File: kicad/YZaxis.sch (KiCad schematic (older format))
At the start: 36 parts, among them CON16 YZ, CON17 Stepstick_Left_Connector, CON18 Stepstick_Right_Connector, CON19 Stepstick_Left_Connector, CON20 Stepstick_Right_Connector, Q5 IRLR2905ZPBF, Q6 FDC6401N, U1 CD4504BPW

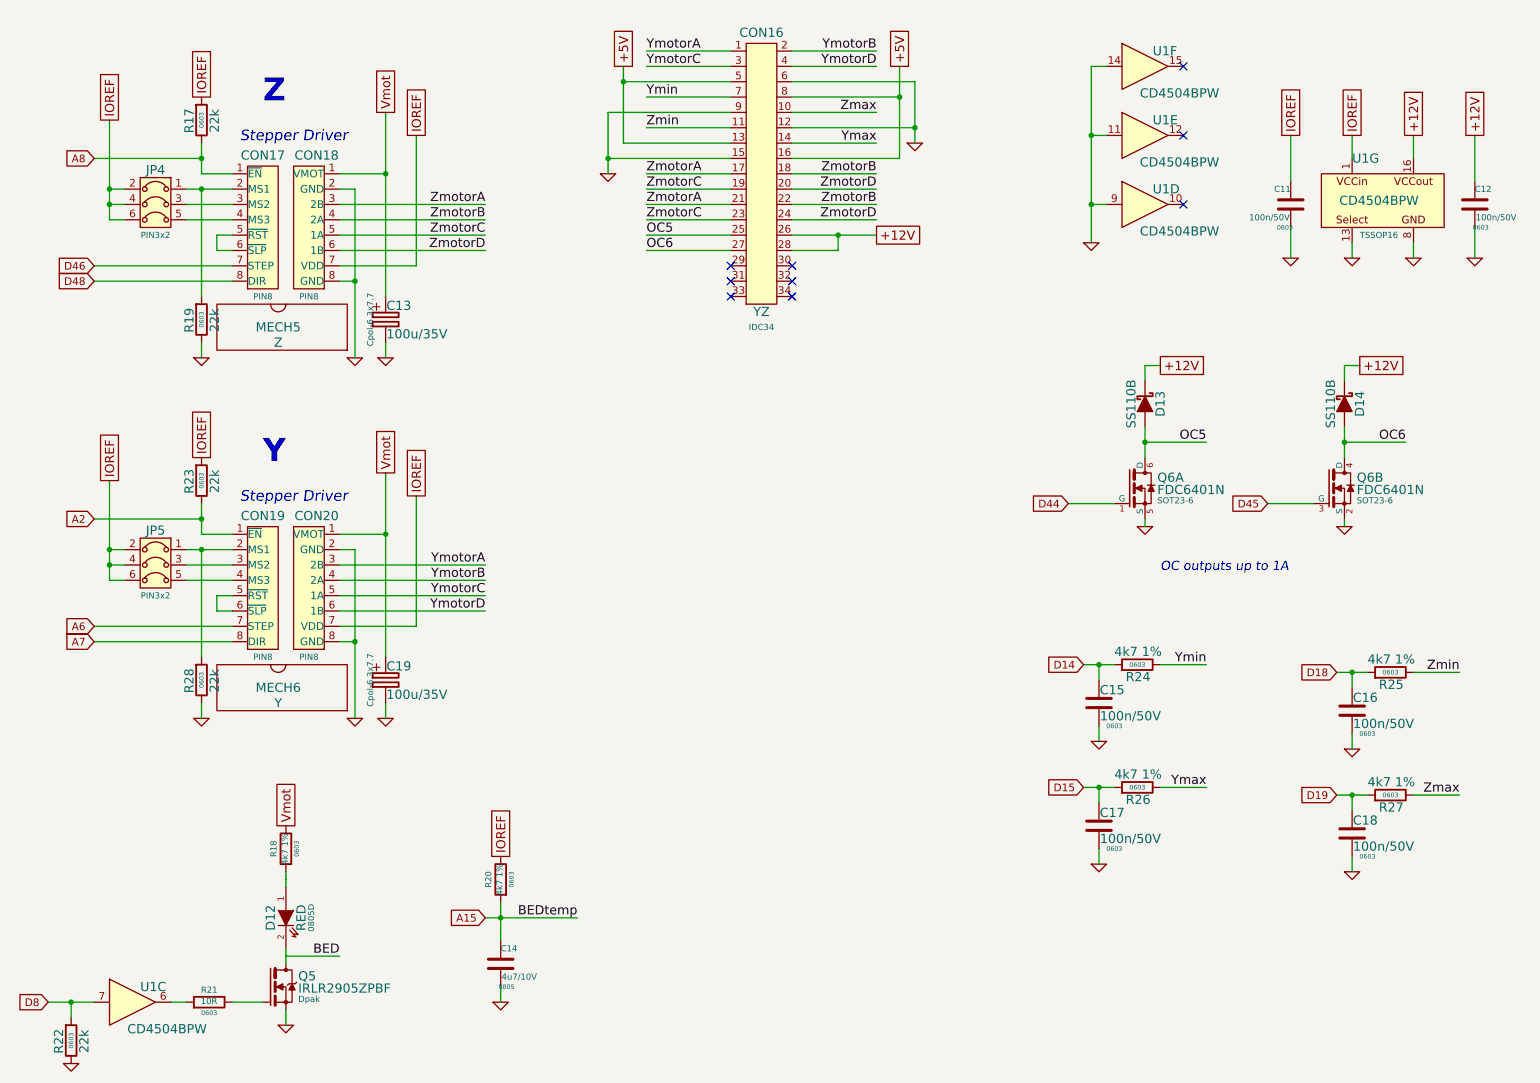
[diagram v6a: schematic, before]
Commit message: Add bed connector. Routing.
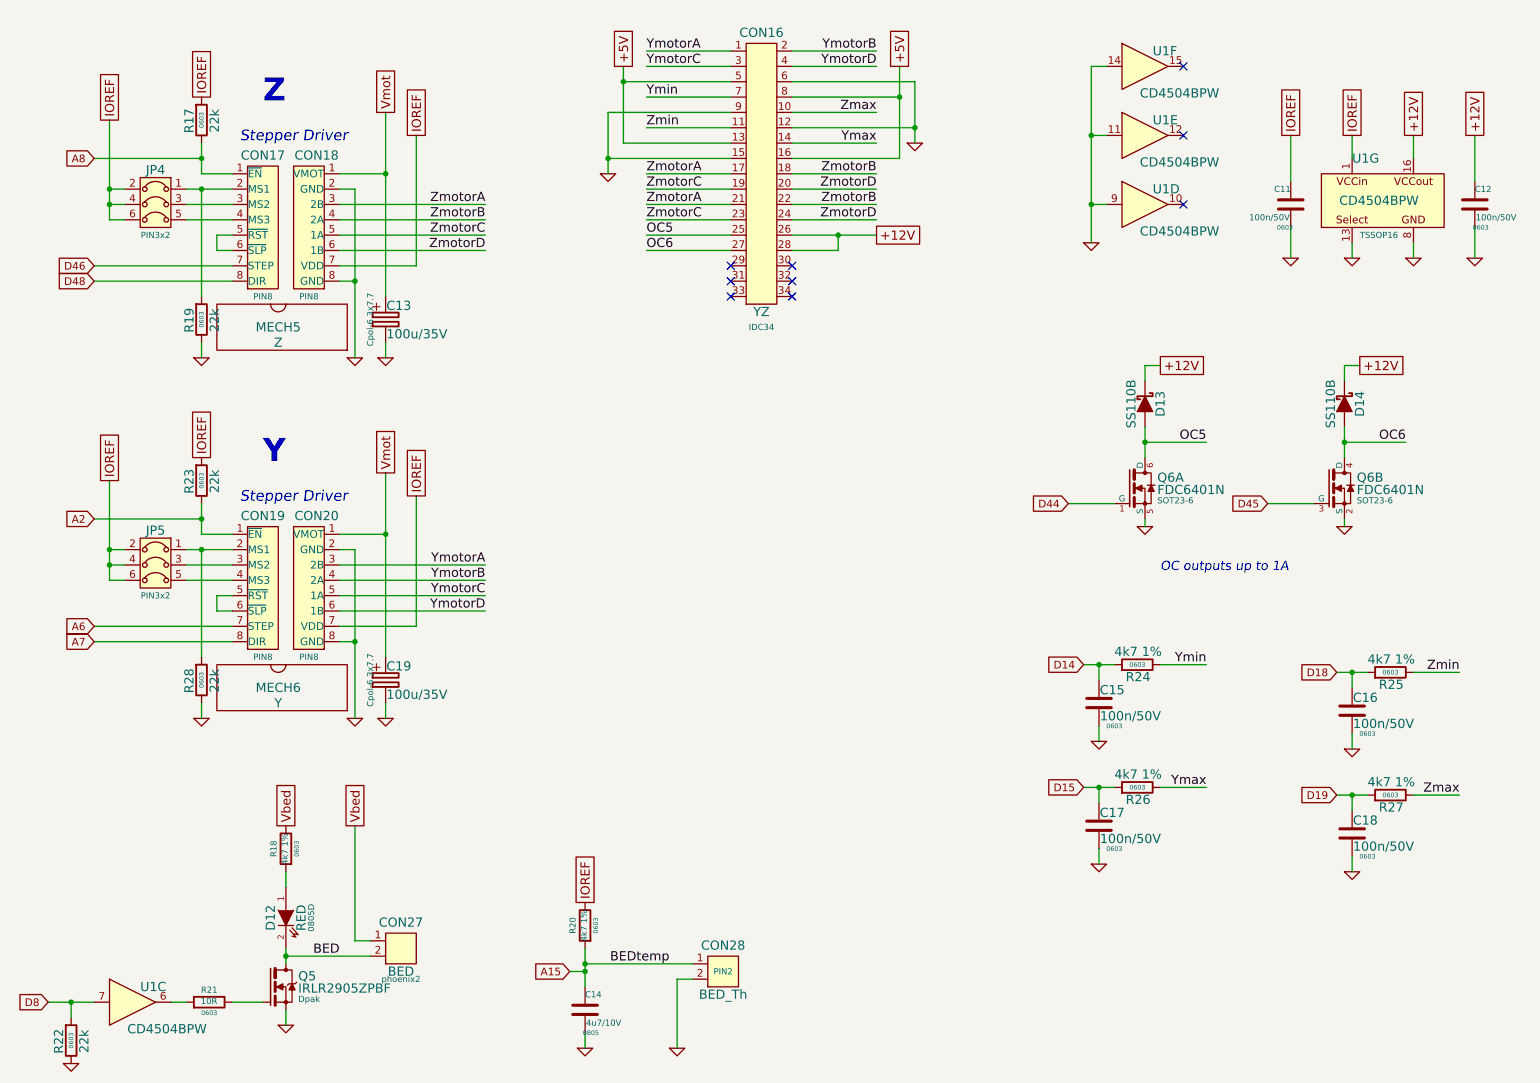
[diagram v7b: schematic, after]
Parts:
- added CON27: BED, phoenix2, symbol CON2
- added CON28: BED_Th, PIN2, symbol CON2
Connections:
- net A15: now also CON28.1
- net BED: now also D12.2 (K), Q5.4 (D), CON27.2
- net GND: now also CON28.2
- net Vmot: no longer R18.2
- new net Vbed: CON27.1, R18.2
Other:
- moved on the sheet: C14, R20
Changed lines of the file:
@@
 L R R20
 U 1 1 534ECA59
-P 3950 6300
-F 0 "R20" V 4030 6300 40  0000 C CNN
-F 1 "4k7 1%" V 3957 6301 40  0000 C CNN
-F 2 "0603" V 3880 6300 30  0000 C CNN
-F 3 "~" H 3950 6300 30  0000 C CNN
-	1    3950 6300
+P 4500 6600
+F 0 "R20" V 4580 6600 40  0000 C CNN
+F 1 "4k7 1%" V 4507 6601 40  0000 C CNN
+F 2 "0603" V 4430 6600 30  0000 C CNN
+F 3 "~" H 4500 6600 30  0000 C CNN
+	1    4500 6600
 	-1   0    0    1
 $EndComp
@@
 L C C14
 U 1 1 534ECB63
-P 3950 6850
-F 0 "C14" H 3950 6950 40  0000 L CNN
-F 1 "4u7/10V" H 3956 6765 40  0000 L CNN
-F 2 "0805" H 3988 6700 30  0000 C CNN
-F 3 "~" H 3950 6850 60  0000 C CNN
-	1    3950 6850
+P 4500 7150
+F 0 "C14" H 4500 7250 40  0000 L CNN
+F 1 "4u7/10V" H 4506 7065 40  0000 L CNN
+F 2 "0805" H 4538 7000 30  0000 C CNN
+F 3 "~" H 4500 7150 60  0000 C CNN
+	1    4500 7150
 	1    0    0    -1
 $EndComp
@@
 L GND #PWR028
 U 1 1 534ECB96
-P 3950 7100
-F 0 "#PWR028" H 3950 7100 30  0001 C CNN
-F 1 "GND" H 3950 7030 30  0001 C CNN
-F 2 "~" H 3950 7100 60  0000 C CNN
-F 3 "~" H 3950 7100 60  0000 C CNN
-	1    3950 7100
-	1    0    0    -1
-$EndComp
-Wire Wire Line
-	3950 7100 3950 7000
-Wire Wire Line
-	3950 6450 3950 6550
-Wire Wire Line
-	3950 6550 3950 6700
-Text GLabel 3850 6550 0    50   Input ~ 0
+P 4500 7400
+F 0 "#PWR028" H 4500 7400 30  0001 C CNN
+F 1 "GND" H 4500 7330 30  0001 C CNN
+F 2 "~" H 4500 7400 60  0000 C CNN
+F 3 "~" H 4500 7400 60  0000 C CNN
+	1    4500 7400
+	1    0    0    -1
+$EndComp
+Wire Wire Line
+	4500 7400 4500 7300
+Wire Wire Line
+	4500 6750 4500 7000
+Text GLabel 4400 6900 0    50   Input ~ 0
 A15
-Wire Wire Line
-	3850 6550 3950 6550
-Wire Wire Line
-	3950 6550 4450 6550
-Connection ~ 3950 6550
+Connection ~ 4500 6850
 $Comp
 L GND #PWR029
@@
 $EndComp
 Wire Wire Line
-	2550 6350 2550 6300
-Wire Wire Line
-	2550 6300 2550 6250
+	2550 6250 2550 6350
 Wire Wire Line
 	2550 6850 2550 6750
@@
 +12V
 Text GLabel 2550 5950 1    60   UnSpc ~ 0
-Vmot
+Vbed
 Text GLabel 9500 1450 1    60   UnSpc ~ 0
 IOREF
 Text GLabel 9100 1450 1    60   UnSpc ~ 0
 IOREF
-Text GLabel 3950 6150 1    60   UnSpc ~ 0
+Text GLabel 4500 6450 1    60   UnSpc ~ 0
 IOREF
 Text Label 3850 4250 2    60   ~ 0
@@
 $EndComp
 Wire Wire Line
-	1000 7100 1150 7100
-Wire Wire Line
-	1150 7100 1300 7100
+	1000 7100 1300 7100
 $Comp
 L GND #PWR032
@@
 $EndComp
 Wire Wire Line
-	7750 4900 7850 4900
-Wire Wire Line
-	7850 4900 7950 4900
+	7750 4900 7950 4900
 Wire Wire Line
 	8250 4900 8550 4900
@@
 $EndComp
 Wire Wire Line
-	7750 5700 7850 5700
-Wire Wire Line
-	7850 5700 7950 5700
+	7750 5700 7950 5700
 Wire Wire Line
 	8250 5700 8550 5700
@@
 $EndComp
 Wire Wire Line
-	9400 4950 9500 4950
-Wire Wire Line
-	9500 4950 9600 4950
+	9400 4950 9600 4950
 Wire Wire Line
 	9900 4950 10200 4950
@@
 $EndComp
 Wire Wire Line
-	9400 5750 9500 5750
-Wire Wire Line
-	9500 5750 9600 5750
+	9400 5750 9600 5750
 Wire Wire Line
 	9900 5750 10200 5750
@@
 	5850 1300 6400 1300
 Wire Wire Line
-	5850 1600 6550 1600
+	6550 1600 5850 1600
 Wire Wire Line
 	6400 1500 5850 1500
@@
 Ymin
 Wire Wire Line
-	4750 1000 4750 1100
-Wire Wire Line
-	4750 1100 4750 1500
+	4750 1000 4750 1500
 $Comp
 L GND #PWR038
@@
 $EndComp
 Wire Wire Line
-	4650 1300 4650 1600
-Wire Wire Line
-	4650 1600 4650 1700
+	4650 1300 4650 1700
 Text Label 6400 1300 2    60   ~ 0
 Zmax
 Wire Wire Line
-	6650 1100 6650 1400
-Wire Wire Line
-	6650 1400 6650 1500
+	6650 1100 6650 1500
 Text Label 4900 1400 0    60   ~ 0
 Zmin
@@
 Ymax
 Wire Wire Line
-	6550 1600 6550 1200
-Wire Wire Line
-	6550 1200 6550 1000
+	6550 1000 6550 1600
 Text Label 4900 1900 0    60   ~ 0
 ZmotorA
@@
 +12V
 Wire Wire Line
-	6400 2100 6150 2100
-Wire Wire Line
-	6150 2100 5850 2100
+	5850 2100 6400 2100
 Wire Wire Line
 	5850 2200 6150 2200
@@
 	7900 1000 7800 1000
 Wire Wire Line
-	7800 1000 7800 1450
-Wire Wire Line
-	7800 1450 7800 1900
-Wire Wire Line
-	7800 1900 7800 2150
+	7800 1000 7800 2150
 Wire Wire Line
 	7900 1900 7800 1900
@@
 	9450 4000 9450 3950
 Wire Wire Line
-	8150 3350 8150 3450
-Wire Wire Line
-	8150 3450 8150 3550
-Wire Wire Line
-	9450 3350 9450 3450
-Wire Wire Line
-	9450 3450 9450 3550
+	8150 3350 8150 3550
+Wire Wire Line
+	9450 3350 9450 3550
 Text GLabel 8250 2950 2    60   UnSpc ~ 0
 +12V
@@
 	2000 1700 2200 1700
 Wire Wire Line
-	1900 1800 2000 1800
-Wire Wire Line
-	2000 1800 2200 1800
+	1900 1800 2200 1800
 Wire Wire Line
 	2200 1900 1900 1900
@@
 	2900 2400 3000 2400
 Wire Wire Line
-	3000 1800 3000 2400
-Wire Wire Line
-	3000 2400 3000 2900
+	3000 1800 3000 2900
 Wire Wire Line
 	3000 1800 2900 1800
@@
 	2900 1700 3200 1700
 Wire Wire Line
-	3200 1300 3200 1700
-Wire Wire Line
-	3200 1700 3200 2500
+	3200 1300 3200 2500
 Wire Wire Line
 	2900 2300 3400 2300
@@
 	3400 2300 3400 1450
 Wire Wire Line
-	2000 1500 2000 1600
-Wire Wire Line
-	2000 1600 2000 1700
+	2000 1500 2000 1700
 Wire Wire Line
 	1300 1600 2000 1600
@@
 	1400 2000 1500 2000
 Wire Wire Line
-	1400 1350 1400 1800
-Wire Wire Line
-	1400 1800 1400 1900
-Wire Wire Line
-	1400 1900 1400 2000
+	1400 1350 1400 2000
 Wire Wire Line
 	1500 1800 1400 1800
@@
 	2000 4050 2200 4050
 Wire Wire Line
-	1900 4150 2000 4150
-Wire Wire Line
-	2000 4150 2200 4150
+	1900 4150 2200 4150
 Wire Wire Line
 	2200 4250 1900 4250
@@
 	2900 4750 3000 4750
 Wire Wire Line
-	3000 4150 3000 4750
-Wire Wire Line
-	3000 4750 3000 5250
+	3000 4150 3000 5250
 Wire Wire Line
 	3000 4150 2900 4150
@@
 	2900 4050 3200 4050
 Wire Wire Line
-	3200 3650 3200 4050
-Wire Wire Line
-	3200 4050 3200 4850
+	3200 3650 3200 4850
 Wire Wire Line
 	2900 4650 3400 4650
@@
 	3400 4650 3400 3800
 Wire Wire Line
-	2000 3850 2000 3950
-Wire Wire Line
-	2000 3950 2000 4050
+	2000 3850 2000 4050
 Wire Wire Line
 	1300 3950 2000 3950
@@
 	1400 4350 1500 4350
 Wire Wire Line
-	1400 3700 1400 4150
-Wire Wire Line
-	1400 4150 1400 4250
-Wire Wire Line
-	1400 4250 1400 4350
+	1400 3700 1400 4350
 Wire Wire Line
 	1500 4150 1400 4150
@@
 	1    0    0    -1
 $EndComp
-Wire Wire Line
-	2550 6800 2900 6800
 Text Label 2900 6800 2    60   ~ 0
 BED
-Text Label 4450 6550 2    60   ~ 0
+Text Label 5050 6850 2    60   ~ 0
 BEDtemp
+$Comp
+L CON2 CON28
+U 1 1 539C896C
+P 5400 6900
+F 0 "CON28" H 5400 7070 60  0000 C CNN
+F 1 "BED_Th" H 5400 6750 60  0000 C CNN
+F 2 "PIN2" H 5400 6900 40  0000 C CNN
+F 3 "" H 5400 6900 40  0000 C CNN
+	1    5400 6900
+	1    0    0    -1
+$EndComp
+$Comp
+L CON2 CON27
+U 1 1 539C8A5D
+P 3300 6750
+F 0 "CON27" H 3300 6920 60  0000 C CNN
+F 1 "BED" H 3300 6600 60  0000 C CNN
+F 2 "phoenix2" H 3300 6550 40  0000 C CNN
+F 3 "" H 3300 6750 40  0000 C CNN
+	1    3300 6750
+	1    0    0    -1
+$EndComp
+Wire Wire Line
+	5200 6950 5100 6950
+Wire Wire Line
+	5100 6950 5100 7400
+$Comp
+L GND #PWR049
+U 1 1 539C8F1D
+P 5100 7400
+F 0 "#PWR049" H 5100 7400 30  0001 C CNN
+F 1 "GND" H 5100 7330 30  0001 C CNN
+F 2 "~" H 5100 7400 60  0000 C CNN
+F 3 "~" H 5100 7400 60  0000 C CNN
+	1    5100 7400
+	1    0    0    -1
+$EndComp
+Wire Wire Line
+	3100 6700 3000 6700
+Wire Wire Line
+	3000 6700 3000 5950
+Text GLabel 3000 5950 1    60   UnSpc ~ 0
+Vbed
+Wire Wire Line
+	3100 6800 2550 6800
+Connection ~ 2550 6800
+Wire Wire Line
+	4500 6850 5200 6850
+Wire Wire Line
+	4400 6900 4500 6900
+Connection ~ 4500 6900
 $EndSCHEMATC

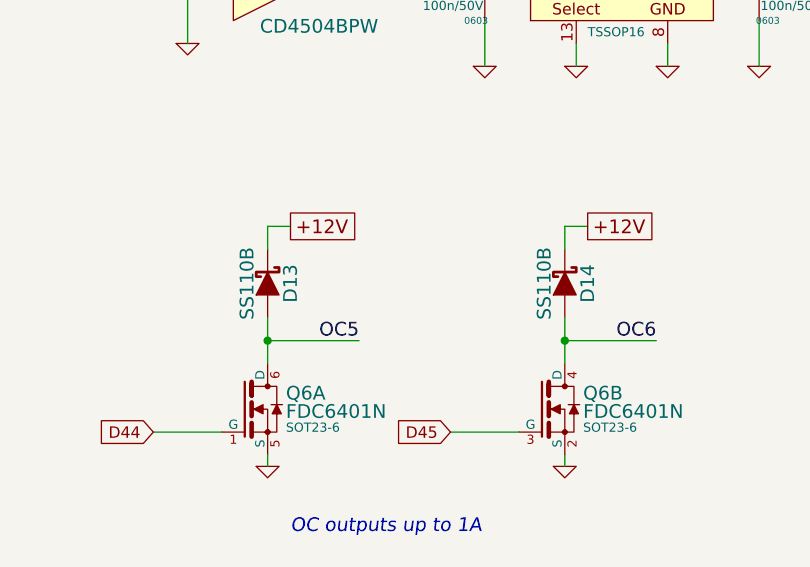
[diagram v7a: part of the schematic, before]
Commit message: Change 1A diodes. Add capacitors next to OC outputs. Place.
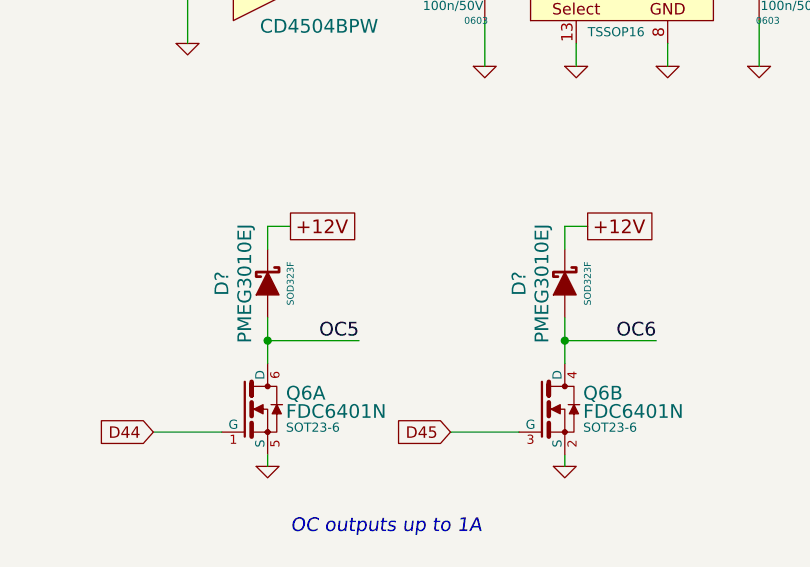
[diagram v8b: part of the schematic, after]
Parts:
- removed D13, D14: SS110B, symbol SS110B
- added D? (x2): PMEG3010EJ, SOD323F, symbol PMEG3010EJ
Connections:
- net +12V: now also D?.1, D?.1
- net OC5: now also D?.2
- net OC6: now also D?.2
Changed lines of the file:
@@
 Text GLabel 8250 2950 2    60   UnSpc ~ 0
 +12V
-$Comp
-L SS110B D13
-U 1 1 53924625
-P 8150 3200
-F 0 "D13" H 8150 3100 60  0000 C CNN
-F 1 "SS110B" H 8150 3290 60  0000 C CNN
-F 2 "" V 8000 3162 30  0000 C CNN
-F 3 "" V 8150 3200 60  0000 C CNN
-	1    8150 3200
-	0    -1   -1   0
-$EndComp
 Wire Wire Line
 	8250 2950 8150 2950
@@
 Text GLabel 9550 2950 2    60   UnSpc ~ 0
 +12V
-$Comp
-L SS110B D14
-U 1 1 5392462F
-P 9450 3200
-F 0 "D14" H 9450 3100 60  0000 C CNN
-F 1 "SS110B" H 9450 3290 60  0000 C CNN
-F 2 "" V 9300 3162 30  0000 C CNN
-F 3 "" V 9450 3200 60  0000 C CNN
-	1    9450 3200
-	0    -1   -1   0
-$EndComp
 Wire Wire Line
 	9550 2950 9450 2950
@@
 	4400 6900 4500 6900
 Connection ~ 4500 6900
+$Comp
+L PMEG3010EJ D?
+U 1 1 539CCE24
+P 8150 3200
+F 0 "D?" H 8150 3400 60  0000 C CNN
+F 1 "PMEG3010EJ" H 8150 3300 60  0000 C CNN
+F 2 "SOD323F" H 8150 3100 30  0000 C CNN
+F 3 "" V 8150 3200 60  0000 C CNN
+	1    8150 3200
+	0    -1   -1   0
+$EndComp
+$Comp
+L PMEG3010EJ D?
+U 1 1 539CD76F
+P 9450 3200
+F 0 "D?" H 9450 3400 60  0000 C CNN
+F 1 "PMEG3010EJ" H 9450 3300 60  0000 C CNN
+F 2 "SOD323F" H 9450 3100 30  0000 C CNN
+F 3 "" V 9450 3200 60  0000 C CNN
+	1    9450 3200
+	0    -1   -1   0
+$EndComp
 $EndSCHEMATC
